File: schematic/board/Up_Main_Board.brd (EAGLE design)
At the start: 79.9 x 73.5 mm, 18 parts

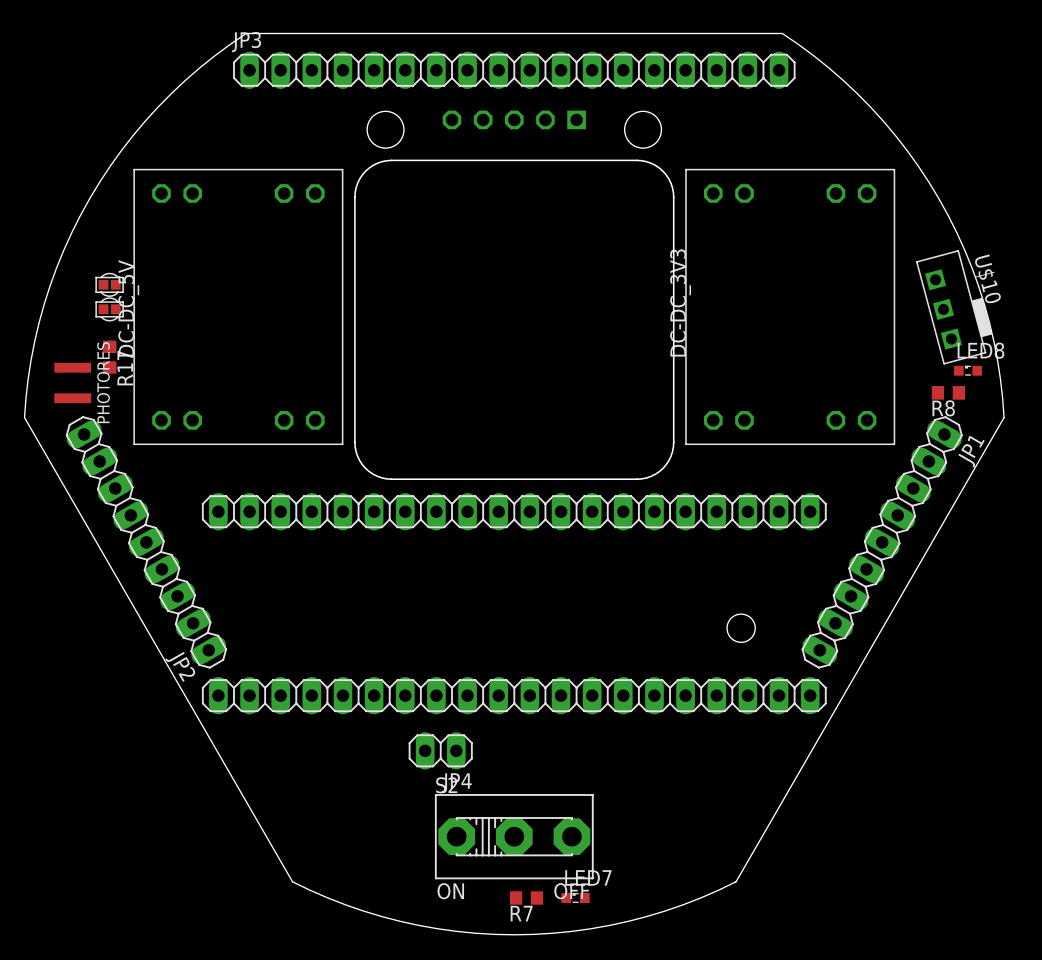
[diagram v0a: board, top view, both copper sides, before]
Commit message: 100501 раз изменил пины на плате
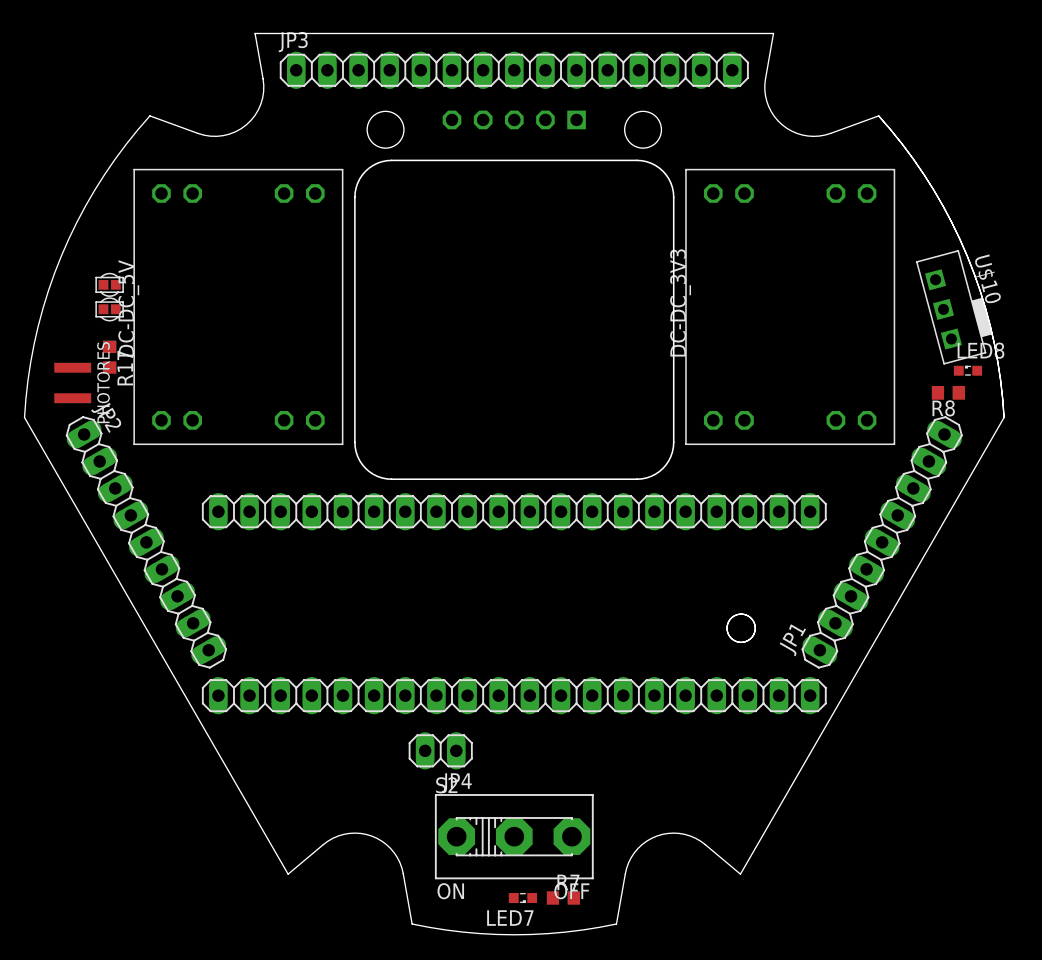
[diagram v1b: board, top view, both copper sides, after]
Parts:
- JP3: device pinhead:1X18 -> pinhead:1X15
- moved LED7 4.30 mm to (50.7, 13.0), turned to 180 degrees
- moved R7 3.00 mm to (54.0, 13.0), turned to 0 degrees
- turned JP1 to 60 degrees
- turned JP2 to 300 degrees
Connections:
- net SPI4_MISO renamed 4MISO
- net SPI4_MOSI renamed 4MOSI
- removed net SDIO_DATA0: U$2.35
- removed net SDIO_DATA1: U$2.25
- removed net SDIO_DATA2: U$2.26
- removed net SDIO_DATA3: U$2.33
- removed net SPI1_MISO: U$2.32
- removed net SPI1_MOSI: U$2.13
- removed net SPI1_SCK: U$2.11
- removed net SPI5_MISO: U$2.29
- removed net SPI5_MOSI: U$2.27
- removed net SPI5_SCK: U$2.14
- new net 1MISO: JP3.3, U$2.32
- new net 1MOSI: JP3.2, U$2.13
- new net 1SCK: JP3.1, U$2.11
- new net 5MISO: JP1.4, JP3.11, U$2.29
- new net 5MOSI: JP1.3, JP3.10, U$2.27
- new net 5SCK: JP1.2, JP3.9, U$2.14
- new net APD_FB_VOLT: JP1.8
- new net APD_PWM: JP1.9
- new net LASER_COMP: JP1.6
- new net N$19: JP3.13
- new net N$20: JP3.14
- new net N$21: JP3.15
- new net SDIO_DAT0: JP2.6, U$2.35
- new net SDIO_DAT1: JP2.7, U$2.25
- new net SDIO_DAT2: JP2.2, U$2.26
- new net SDIO_DAT3: JP2.3, U$2.33
- new net TDC_INT: JP1.7
- new net USIL_ON: JP1.1
- net 3V3: now also JP3.5
- net 5V: now also JP2.1
- net CE_NRF: now also JP3.7
- net CS_LIS: now also JP3.4
- net CS_LSM: now also JP3.12
- net CS_NRF: now also JP3.8
- net CS_TDC: now also JP1.5
- net GND: now also JP3.6
- net SCL: now also JP2.9
- net SDA: now also JP2.8
- net SDIO_CK: now also JP2.5
- net SDIO_CMD: now also JP2.4
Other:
- outline, holes or cut-outs redrawn

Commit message: Развод на плате...
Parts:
- U$3: device NEON-BLADE-2024:GPS_NEO7M_W-PPS_&_ANT -> NEON-BLADE-2023:GPS_NEO7M_W-PPS_&_ANT
- moved LED8 1.00 mm to (86.0, 56.0)
- moved R8 1.00 mm to (84.4, 54.2)
- moved U$2 0.30 mm to (50.0, 36.7)
- moved U$3 0.10 mm to (50.0, 58.1)
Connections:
- removed net N$2: DC-DC_5V.P$3, DC-DC_5V.P$4
- removed net N$3: DC-DC_3V3.P$3, DC-DC_3V3.P$4
- removed net SPI4_SCK: U$2.22
- new net 4SCK: JP1.2, U$2.22
- net 4MISO: now also JP1.4
- net 4MOSI: now also JP1.3
- net 5MISO: no longer JP1.4
- net 5MOSI: no longer JP1.3
- net 5SCK: no longer JP1.2
- net GND: now also DC-DC_3V3.P$3, DC-DC_3V3.P$4, DC-DC_5V.P$3, DC-DC_5V.P$4
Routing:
- net GND: track 0.00 -> 230.6 mm, vias 0 -> 2
- net 3V3: track 0.00 -> 154.7 mm, vias 0 -> 4
- net V_BAT: track 0.00 -> 115.2 mm, vias 0 -> 1
- net GPS_TX: track 0.00 -> 89.2 mm, vias 0 -> 1
- net 5MOSI: track 0.00 -> 89.0 mm, vias 0 -> 3
- net 1MISO: track 0.00 -> 84.2 mm
- net GPS_RX: track 0.00 -> 83.8 mm, vias 0 -> 1
- net 5MISO: track 0.00 -> 83.5 mm, vias 0 -> 3
- net CS_LIS: track 0.00 -> 63.5 mm
- net CE_NRF: track 0.00 -> 55.9 mm
- net 5V: track 0.00 -> 55.8 mm, vias 0 -> 1
- net 1SCK: track 0.00 -> 55.5 mm
- net 5SCK: track 0.00 -> 54.9 mm, vias 0 -> 1
- net SDIO_DAT3: track 0.00 -> 53.3 mm
- net 4SCK: track 0.00 -> 51.4 mm, vias 0 -> 2
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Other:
- outline, holes or cut-outs redrawn

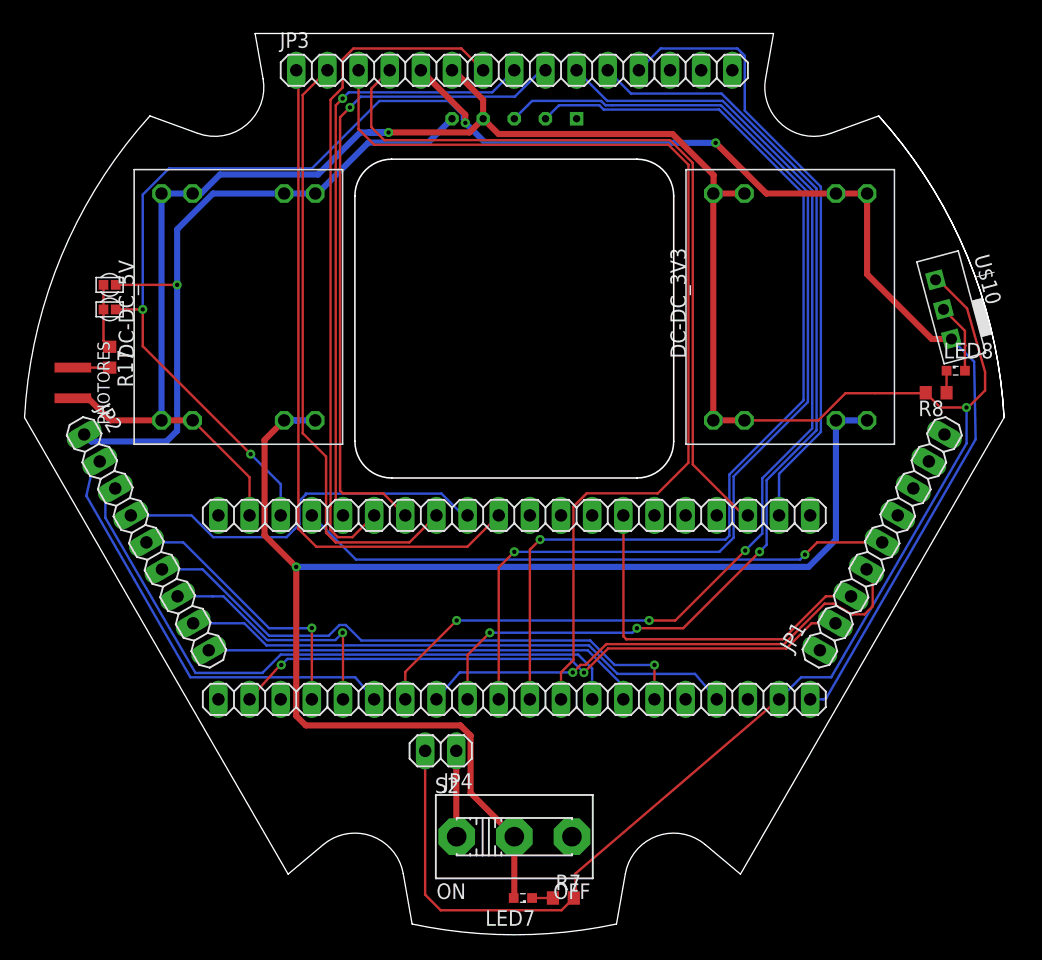
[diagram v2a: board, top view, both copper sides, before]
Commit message: поменял гпс на верхней плате
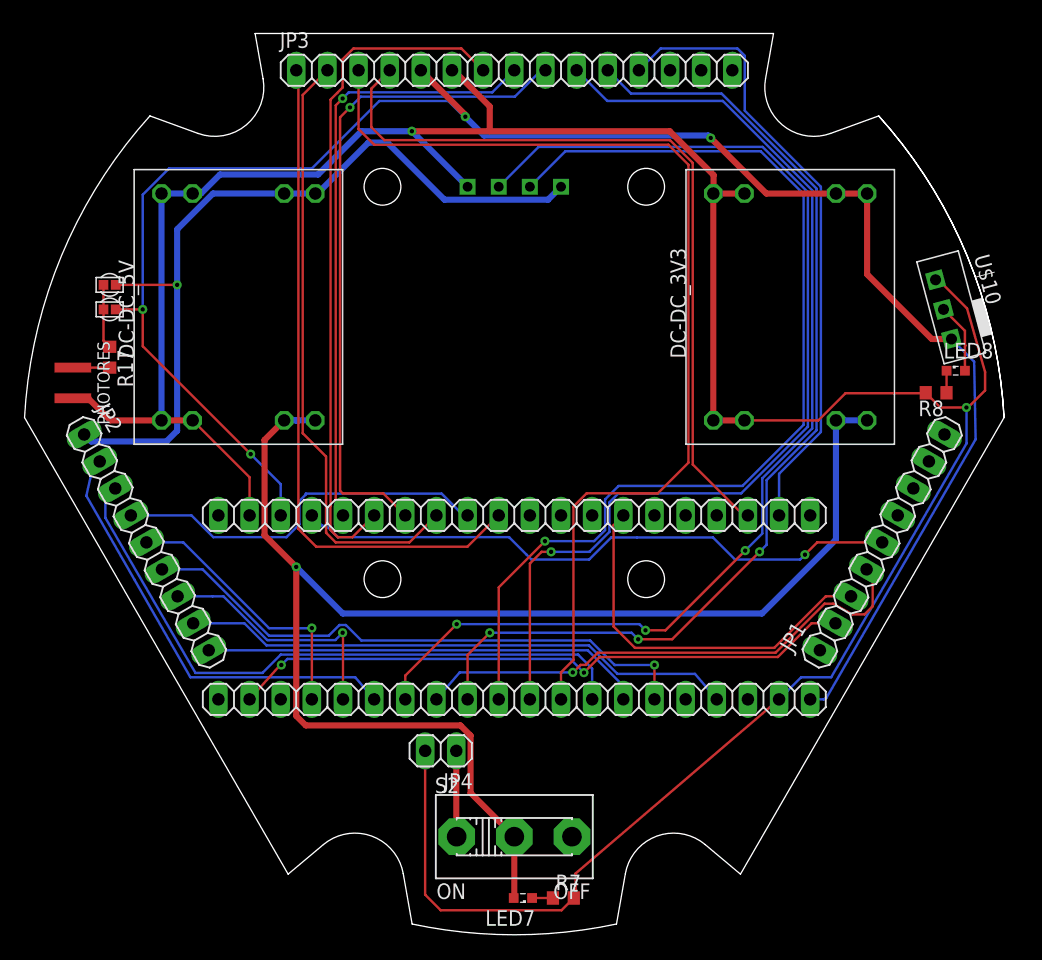
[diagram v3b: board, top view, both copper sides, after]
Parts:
- removed U$3: GPS_NEO7M_W-PPS, NEON-BLADE-2023:GPS_NEO7M_W-PPS_&_ANT
- added U$5: GPS, cansat-lib:GPS
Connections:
- net 5V: now also U$5.UCC; no longer U$3.VCC
- net GND: now also U$5.GND; no longer U$3.GND
- net GPS_RX: now also U$5.TX; no longer U$3.RX
- net GPS_TX: now also U$5.RX; no longer U$3.TX
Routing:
- net 5V: track 55.8 -> 66.2 mm
- net GND: track 230.6 -> 235.8 mm
- net GPS_TX: track 89.2 -> 84.7 mm
- net GPS_RX: track 83.8 -> 87.0 mm
- net V_BAT: track 115.2 -> 118.4 mm
- net CS_TDC: track 48.6 -> 50.1 mm
- net 3V3: track 154.7 -> 154.0 mm
- net 4MOSI: track 30.6 -> 31.2 mm

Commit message: спонсор страданий
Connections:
- removed net N$20: JP3.14
- net V_BAT: now also JP3.14
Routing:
- net V_BAT: track 118.4 -> 160.8 mm
- net CS_LSM: track 51.1 -> 46.4 mm
- net GPS_RX: track 87.0 -> 86.4 mm
- net 5MISO: track 83.9 -> 83.3 mm
- net 5MOSI: track 89.2 -> 88.6 mm
- net GPS_TX: track 84.7 -> 84.1 mm
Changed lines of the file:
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@@
 <wire x1="68.6" y1="46.6" x2="73.5904" y2="51.5904" width="0.2" layer="16"/>
 <wire x1="57.4044" y1="45.5044" x2="58.5" y2="46.6" width="0.2" layer="16"/>
-<wire x1="73.5904" y1="51.5904" x2="73.5904" y2="70.4096" width="0.2" layer="16"/>
-<wire x1="73.5904" y1="70.4096" x2="70.089884375" y2="73.8984125" width="0.2" layer="16"/>
+<wire x1="73.5904" y1="51.5904" x2="73.5904" y2="69.41294375" width="0.2" layer="16"/>
+<wire x1="73.5904" y1="69.41294375" x2="69.089884375" y2="73.8984125" width="0.2" layer="16"/>
 <wire x1="54.1684125" y1="73.8984125" x2="51.27" y2="71" width="0.2" layer="16"/>
-<wire x1="70.089884375" y1="73.8984125" x2="54.1684125" y2="73.8984125" width="0.2" layer="16"/>
+<wire x1="69.089884375" y1="73.8984125" x2="54.1684125" y2="73.8984125" width="0.2" layer="16"/>
 <wire x1="56.5044" y1="42.1" x2="57.4044" y2="43" width="0.2" layer="16"/>
 <wire x1="52.5" y1="42.1" x2="56.5044" y2="42.1" width="0.2" layer="16"/>
@@
 <wire x1="52.2306" y1="41.2306" x2="53" y2="41.2306" width="0.2" layer="1"/>
 <via x="53" y="41.2306" extent="1-16" drill="0.35"/>
-<wire x1="73.9428" y1="51.441175" x2="73.9428" y2="70.558825" width="0.2" layer="16"/>
-<wire x1="70.2508125" y1="74.2508125" x2="51.9808125" y2="74.2508125" width="0.2" layer="16"/>
+<wire x1="73.9428" y1="51.441175" x2="73.9428" y2="69.558825" width="0.2" layer="16"/>
+<wire x1="69.2508125" y1="74.2508125" x2="51.9808125" y2="74.2508125" width="0.2" layer="16"/>
 <wire x1="51.9808125" y1="74.2508125" x2="48.73" y2="71" width="0.2" layer="16"/>
-<wire x1="73.9428" y1="70.558825" x2="70.2508125" y2="74.2508125" width="0.2" layer="16"/>
+<wire x1="73.9428" y1="69.558825" x2="69.2508125" y2="74.2508125" width="0.2" layer="16"/>
 <wire x1="57.7568" y1="45.26338125" x2="58.49341875" y2="46" width="0.2" layer="16"/>
 <wire x1="57.7568" y1="42.854025" x2="57.7568" y2="45.26338125" width="0.2" layer="16"/>
@@
 <contactref element="U$2" pad="29"/>
 <contactref element="JP3" pad="11"/>
-<wire x1="57.62" y1="80.5" x2="59.52" y2="78.6" width="0.2" layer="16"/>
-<wire x1="59.52" y1="78.6" x2="66.901625" y2="78.6" width="0.2" layer="16"/>
-<wire x1="66.901625" y1="78.6" x2="74.6476" y2="70.854025" width="0.2" layer="16"/>
-<wire x1="74.6476" y1="70.854025" x2="74.6476" y2="51.145975" width="0.2" layer="16"/>
+<wire x1="57.62" y1="80.5" x2="61.52" y2="76.6" width="0.2" layer="16"/>
+<wire x1="61.52" y1="76.6" x2="67.901625" y2="76.6" width="0.2" layer="16"/>
+<wire x1="67.901625" y1="76.6" x2="74.6476" y2="69.854025" width="0.2" layer="16"/>
+<wire x1="74.6476" y1="69.854025" x2="74.6476" y2="51.145975" width="0.2" layer="16"/>
 <wire x1="74.6476" y1="51.145975" x2="70.5756" y2="47.073975" width="0.2" layer="16"/>
 <wire x1="70.5756" y1="41.8062" x2="70" y2="41.2306" width="0.2" layer="16"/>
@@
 <contactref element="U$2" pad="27"/>
 <contactref element="JP3" pad="10"/>
-<wire x1="55.08" y1="80.5" x2="57.58" y2="78" width="0.2" layer="16"/>
-<wire x1="57.58" y1="78" x2="67" y2="78" width="0.2" layer="16"/>
-<wire x1="67" y1="78" x2="74.2952" y2="70.7048" width="0.2" layer="16"/>
-<wire x1="74.2952" y1="70.7048" x2="74.2952" y2="51.2952" width="0.2" layer="16"/>
+<wire x1="55.08" y1="80.5" x2="59.58" y2="76" width="0.2" layer="16"/>
+<wire x1="59.58" y1="76" x2="68" y2="76" width="0.2" layer="16"/>
+<wire x1="68" y1="76" x2="74.2952" y2="69.7048" width="0.2" layer="16"/>
+<wire x1="74.2952" y1="69.7048" x2="74.2952" y2="51.2952" width="0.2" layer="16"/>
 <wire x1="74.2952" y1="51.2952" x2="70.2232" y2="47.2232" width="0.2" layer="16"/>
 <wire x1="70.2232" y1="47.2232" x2="70.2232" y2="42.7232" width="0.2" layer="16"/>
@@
 <wire x1="71.59" y1="44.2" x2="71.59" y2="47.59" width="0.2" layer="16"/>
 <wire x1="71.59" y1="47.59" x2="75" y2="51" width="0.2" layer="16"/>
-<wire x1="75" y1="51" x2="75" y2="71" width="0.2" layer="16"/>
-<wire x1="68.7944" y1="81.68218125" x2="68.20018125" y2="82.2764" width="0.2" layer="16"/>
-<wire x1="68.7944" y1="77.2056" x2="68.7944" y2="81.68218125" width="0.2" layer="16"/>
-<wire x1="61.9364" y1="82.2764" x2="60.16" y2="80.5" width="0.2" layer="16"/>
-<wire x1="75" y1="71" x2="68.7944" y2="77.2056" width="0.2" layer="16"/>
-<wire x1="68.20018125" y1="82.2764" x2="61.9364" y2="82.2764" width="0.2" layer="16"/>
+<wire x1="75" y1="70" x2="75" y2="51" width="0.2" layer="16"/>
+<wire x1="60.16" y1="80.5" x2="63.7076" y2="76.9524" width="0.2" layer="16"/>
+<wire x1="63.7076" y1="76.9524" x2="68.0476" y2="76.9524" width="0.2" layer="16"/>
+<wire x1="68.0476" y1="76.9524" x2="75" y2="70" width="0.2" layer="16"/>
 </signal>
 <signal name="5V">
@@
 <wire x1="46.4344" y1="21.5656" x2="46.4344" y2="26.2443125" width="0.5" layer="1"/>
 <wire x1="46.4344" y1="26.2443125" x2="45.6051125" y2="27.0736" width="0.5" layer="1"/>
-<wire x1="76.23" y1="51.95" x2="78.77" y2="51.95" width="0.5" layer="16"/>
-<wire x1="76.23" y1="42.23" x2="70.2" y2="36.2" width="0.5" layer="16"/>
-<wire x1="76.23" y1="42.23" x2="76.23" y2="51.95" width="0.5" layer="16"/>
+<wire x1="80.53" y1="46.53" x2="70.2" y2="36.2" width="0.5" layer="16"/>
 <wire x1="45.6051125" y1="27.0736" x2="32.9964875" y2="27.0736" width="0.5" layer="1"/>
 <wire x1="32.9964875" y1="27.0736" x2="32.2144" y2="27.8556875" width="0.5" layer="1"/>
@@
 <wire x1="29.63" y1="50.35" x2="29.63" y2="42.5844" width="0.5" layer="1"/>
 <wire x1="32.2144" y1="40" x2="29.63" y2="42.5844" width="0.5" layer="1"/>
+<contactref element="JP3" pad="14"/>
+<wire x1="80.53" y1="46.53" x2="80.53" y2="51.95" width="0.5" layer="16"/>
+<wire x1="80.53" y1="51.95" x2="80.53" y2="70.77" width="0.5" layer="16"/>
+<wire x1="80.53" y1="70.77" x2="78.3" y2="73" width="0.5" layer="16"/>
+<wire x1="72.89180625" y1="73" x2="78.3" y2="73" width="0.5" layer="16"/>
+<wire x1="65.24" y1="80.5" x2="65.24" y2="79.2148" width="0.5" layer="16"/>
+<wire x1="65.24" y1="79.2148" x2="67" y2="77.4548" width="0.5" layer="16"/>
+<wire x1="67" y1="77.4548" x2="68.43700625" y2="77.4548" width="0.5" layer="16"/>
+<wire x1="68.43700625" y1="77.4548" x2="72.89180625" y2="73" width="0.5" layer="16"/>
+<wire x1="76.23" y1="51.95" x2="78.77" y2="51.95" width="0.5" layer="16"/>
+<wire x1="78.77" y1="51.95" x2="78.82" y2="51.95" width="0.5" layer="16"/>
+<wire x1="78.82" y1="51.95" x2="80.53" y2="51.95" width="0.5" layer="16"/>
 </signal>
 <signal name="PHOTORES">
@@
 <contactref element="JP3" pad="13"/>
 </signal>
-<signal name="N$20">
-<contactref element="JP3" pad="14"/>
-</signal>
 <signal name="N$21">

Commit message: почти добавил новый разъём
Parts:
- removed JP1, JP2: (no value), pinhead:1X09
- removed JP3: (no value), pinhead:1X15
- added U$6, U$7: PBS_SMD_X9, NEON-BLADE-2024:PBS_SMD_X9
- added U$8: PBS_SMD_X15, NEON-BLADE-2024:PBD_SMD_X15
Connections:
- removed net N$19: JP3.13
- removed net N$21: JP3.15
- new net N$2: U$8.13
- new net N$3: U$8.15
- net 1MISO: now also U$8.3; no longer JP3.3
- net 1MOSI: now also U$8.2; no longer JP3.2
- net 1SCK: now also U$8.1; no longer JP3.1
- net 3V3: now also U$8.5; no longer JP3.5
- net 4MISO: now also U$6.4; no longer JP1.4
- net 4MOSI: now also U$6.3; no longer JP1.3
- net 4SCK: now also U$6.2; no longer JP1.2
- net 5MISO: now also U$8.11; no longer JP3.11
- net 5MOSI: now also U$8.10; no longer JP3.10
- net 5SCK: now also U$8.9; no longer JP3.9
- net 5V: now also U$7.1; no longer JP2.1
- net APD_FB_VOLT: now also U$6.8; no longer JP1.8
- net APD_PWM: now also U$6.9; no longer JP1.9
- net CE_NRF: now also U$8.7; no longer JP3.7
- net CS_LIS: now also U$8.4; no longer JP3.4
- net CS_LSM: now also U$8.12; no longer JP3.12
- net CS_NRF: now also U$8.8; no longer JP3.8
- net CS_TDC: now also U$6.5; no longer JP1.5
- net GND: now also U$8.6; no longer JP3.6
- net LASER_COMP: now also U$6.6; no longer JP1.6
- net SCL: now also U$7.9; no longer JP2.9
- net SDA: now also U$7.8; no longer JP2.8
- net SDIO_CK: now also U$7.5; no longer JP2.5
- net SDIO_CMD: now also U$7.4; no longer JP2.4
- net SDIO_DAT0: now also U$7.6; no longer JP2.6
- net SDIO_DAT1: now also U$7.7; no longer JP2.7
- net SDIO_DAT2: now also U$7.2; no longer JP2.2
- net SDIO_DAT3: now also U$7.3; no longer JP2.3
- net TDC_INT: now also U$6.7; no longer JP1.7
- net USIL_ON: now also U$6.1; no longer JP1.1
- net V_BAT: now also U$8.14; no longer JP3.14
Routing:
- net 5SCK: track 54.9 -> 38.4 mm
- net CE_NRF: track 55.9 -> 50.4 mm, vias 0 -> 1
- net 4MISO: track 42.6 -> 37.5 mm, vias 1 -> 2
- net 5V: track 66.2 -> 70.5 mm, vias 1 -> 2
- net 3V3: track 154.0 -> 158.1 mm, vias 4 -> 3
- net 1MISO: track 84.2 -> 88.3 mm, vias 0 -> 1
- net 1SCK: track 55.5 -> 59.5 mm, vias 0 -> 1
- net GND: track 235.8 -> 239.8 mm, vias 2 -> 1
- net CS_LSM: track 46.4 -> 50.1 mm
- net GPS_RX: track 86.4 -> 82.8 mm
- net GPS_TX: track 84.1 -> 80.5 mm
- net 5MOSI: track 88.6 -> 91.6 mm
- net 1MOSI: track 49.6 -> 52.5 mm, vias 0 -> 1
- net SDIO_DAT2: track 36.0 -> 38.1 mm
- net SDIO_DAT0: track 46.9 -> 44.8 mm
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
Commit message: переделки по плате
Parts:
- added JP1: (no value), pinhead:1X02
- added R4: 2k, rcl:R0603
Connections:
- net N$2 renamed COMP_DAC
- new net LED: R4.1, U$2.23
- new net N$37: JP1.2, R4.2
- net 3V3: now also JP1.1
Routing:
- net 3V3: track 158.1 -> 181.2 mm, vias 3 -> 4
- net LED: track 0.00 -> 10.9 mm
- net N$37: track 0.00 -> 5.79 mm
- net SDIO_CMD: track 29.7 -> 30.7 mm
- net 4SCK: track 50.2 -> 50.8 mm

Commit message: ПЕРЕДЕЛАЙ ПАЛТЫ
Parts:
- removed 3V3, 5V: (no value), NEON-BLADE-2023:VIAS-CONNECT
- R17: value 191k/2k -> 2k
- moved S2 7.50 mm to (50.0, 25.5)
- moved PHOTORES 4.49 mm to (15.3, 59.3), turned to 75 degrees
- moved JP4 3.81 mm to (40.5, 23.5)
- moved R4 3.31 mm to (36.7, 25.3)
- moved R17 2.85 mm to (17.9, 59.8)
- moved U$10 2.29 mm to (83.8, 59.0)
- moved R8 2.00 mm to (82.4, 54.1)
- moved LED8 1.63 mm to (86.3, 54.4)
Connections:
- removed net N$13: 3V3.2, 5V.1, R17.1
- net 3V3: now also R17.1; no longer 3V3.1
- net 5V: no longer 5V.2
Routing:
- net 5V: track 70.5 -> 61.4 mm, vias 2 -> 0
- net V_BAT: track 161.0 -> 168.8 mm
- net N$13: track 5.26 -> 0.00 mm
- net LED: track 10.9 -> 7.48 mm
- net N$37: track 5.79 -> 2.62 mm
- net N$1: track 7.01 -> 4.36 mm
- net STATE: track 5.74 -> 7.92 mm
- net N$10: track 1.80 -> 2.42 mm
- net GND: track 239.8 -> 240.4 mm
- net 3V3: track 181.2 -> 181.7 mm
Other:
- outline, holes or cut-outs redrawn
